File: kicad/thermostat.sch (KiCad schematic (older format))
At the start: 80 parts, among them IC1 LM2596S-5, J1 Conn_01x05, J2 Conn_02x02_Top_Bottom, J3 Conn_01x04, J4 Conn_01x04, J6 Screw_Terminal_01x05, SW1 Button, SW2 Button, SW3 Button, SW4 Button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

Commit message: routed board
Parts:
- removed C11: 25F, Capacitor_THT:CP_Radial_D18.0mm_P7.50mm, symbol Device:CP
- removed C12: 2.2uF, Capacitor_SMD:C_0805_2012Metric, symbol Device:C
- removed C13, C14: 100uF, Capacitor_SMD:C_0805_2012Metric, symbol Device:C
- removed C15, C16: 100nF, Capacitor_SMD:C_0805_2012Metric, symbol Device:C
- removed D44, D45, D46: Green, LED_SMD:LED_0805_2012Metric, symbol Device:LED
- removed J2: Conn_02x02_Top_Bottom, Connector_PinHeader_2.54mm:PinHeader_2x02_P2.54mm_Vertical, symbol Connector_Generic:Conn_02x02_Top_Bottom
- removed L2: 2.2uH, Inductor_SMD:L_Coilcraft_XAL5030, symbol Device:L
- removed R10: 120k, Resistor_SMD:R_0805_2012Metric, symbol Device:R_US
- removed R11: 39k, Resistor_SMD:R_0805_2012Metric, symbol Device:R_US
- removed R12, R44, R45, R46: 1k, Resistor_SMD:R_0805_2012Metric, symbol Device:R_US
- removed R13: 294k, Resistor_SMD:R_0805_2012Metric, symbol Device:R_US
- removed R14: 698k, Resistor_SMD:R_0805_2012Metric, symbol Device:R_US
- removed R15: 1050k, Resistor_SMD:R_0805_2012Metric, symbol Device:R_US
- removed R16: 200k, Resistor_SMD:R_0805_2012Metric, symbol Device:R_US
- removed R18: 10m, Resistor_SMD:R_0805_2012Metric, symbol Device:R_US
- removed T1, T2: SIR434DN, Package_SO:Vishay_PowerPAK_1212-8_Single, symbol Transistor_FET:BUK9M9R1-40EX
- removed U11: LTC4041, project_footprints:ltc4041, symbol thermostat-rescue:LTC4041-thermostat
- added J2: Conn_01x03, Connector_PinHeader_2.54mm:PinHeader_1x03_P2.54mm_Vertical, symbol Connector_Generic:Conn_01x03
- added R57: 10k, Resistor_SMD:R_0805_2012Metric, symbol Device:R_US
- J1: value Conn_01x05 -> Conn_01x04; footprint Connector_PinHeader_2.54mm:PinHeader_1x05_P2.54mm_Vertical -> Connector_PinHeader_2.54mm:PinHeader_1x04_P2.54mm_Vertical; symbol Connector_Generic:Conn_01x05 -> Connector_Generic:Conn_01x04
- J3, J4: value Conn_01x04 -> Conn_01x05; footprint Connector_PinHeader_2.54mm:PinHeader_1x04_P2.54mm_Vertical -> Connector_PinHeader_2.54mm:PinHeader_1x05_P2.54mm_Vertical; symbol Connector_Generic:Conn_01x04 -> Connector_Generic:Conn_01x05
- MK5: footprint MountingHole:MountingHole_5mm_Pad -> MountingHole:MountingHole_5mm
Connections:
- net BTNS_GND: now also J4.3 (Pin_3); no longer J4.2 (Pin_2)
- net BTNS_INT: now also J4.1 (Pin_1), R57.1; no longer U1.15 (INTB)
- net BTNS_PWR_3V3: now also J4.2 (Pin_2); no longer J4.1 (Pin_1)
- net BTNS_SCL: now also J4.5 (Pin_5); no longer J4.4 (Pin_4)
- net BTNS_SDA: now also J4.4 (Pin_4); no longer J4.3 (Pin_3)
- net GND: now also J3.3 (Pin_3), J2.3 (Pin_3); no longer J3.2 (Pin_2)
- net GPIO17(GEN0): now also J3.1 (Pin_1)
- net GPIO2(SDA1): now also J1.3 (Pin_3), J3.4 (Pin_4); no longer J1.4 (Pin_4), J3.3 (Pin_3)
- net GPIO3(SCL1): now also J1.4 (Pin_4), J3.5 (Pin_5); no longer J1.5 (Pin_5), J3.4 (Pin_4)
- net PWR_3.3V: now also J3.2 (Pin_2); no longer J3.1 (Pin_1)
- net PWR_5V: now also J1.2 (Pin_2), J2.2 (Pin_2); no longer J1.3 (Pin_3)
- net PWR_5V_RAW: now also J2.1 (Pin_1)
- net at U1.16 (INTA): now also R57.2
- no-connect marks 35 -> 32
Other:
- note added: "## BMP addr=0x76 ##"
- note added: "## GPIO addr=0x20 ##"
- note added: "## LCD addr=0x27 ##"
- note removed: "## addr=0x20 ##"
- note removed: "## addr=0x27 ##"
- note removed: "## addr=0x76 ##"
- note removed: "*1"
- note removed: "*1) V(chg) = Voltage divider, sets supercap charge voltage\n = 0.8 * (1+698k/294k) = 2.7V\n*2) I(chg) = Resistor program, sets supercap charge current\n = 2000/1k = 1a\n*3) V(in) = Voltage divider, sets input min voltage before power fail\n = 1.19 * (1 + 120k/39k) = 4.85V\n*4) I(syslim) = Resistor program, sets input current limit\n = 25mV/10m = 2.5a\n*5) V(sys) = Voltage divider, sets boost conv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"
- note removed: "*2"
- note removed: "*3"
- note removed: "*4"
- note removed: "*5"
- note removed: "*6"
- moved on the sheet: C1, C2, D1, D2, D40, D41, D42, D43, D47, D51, D52, IC1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

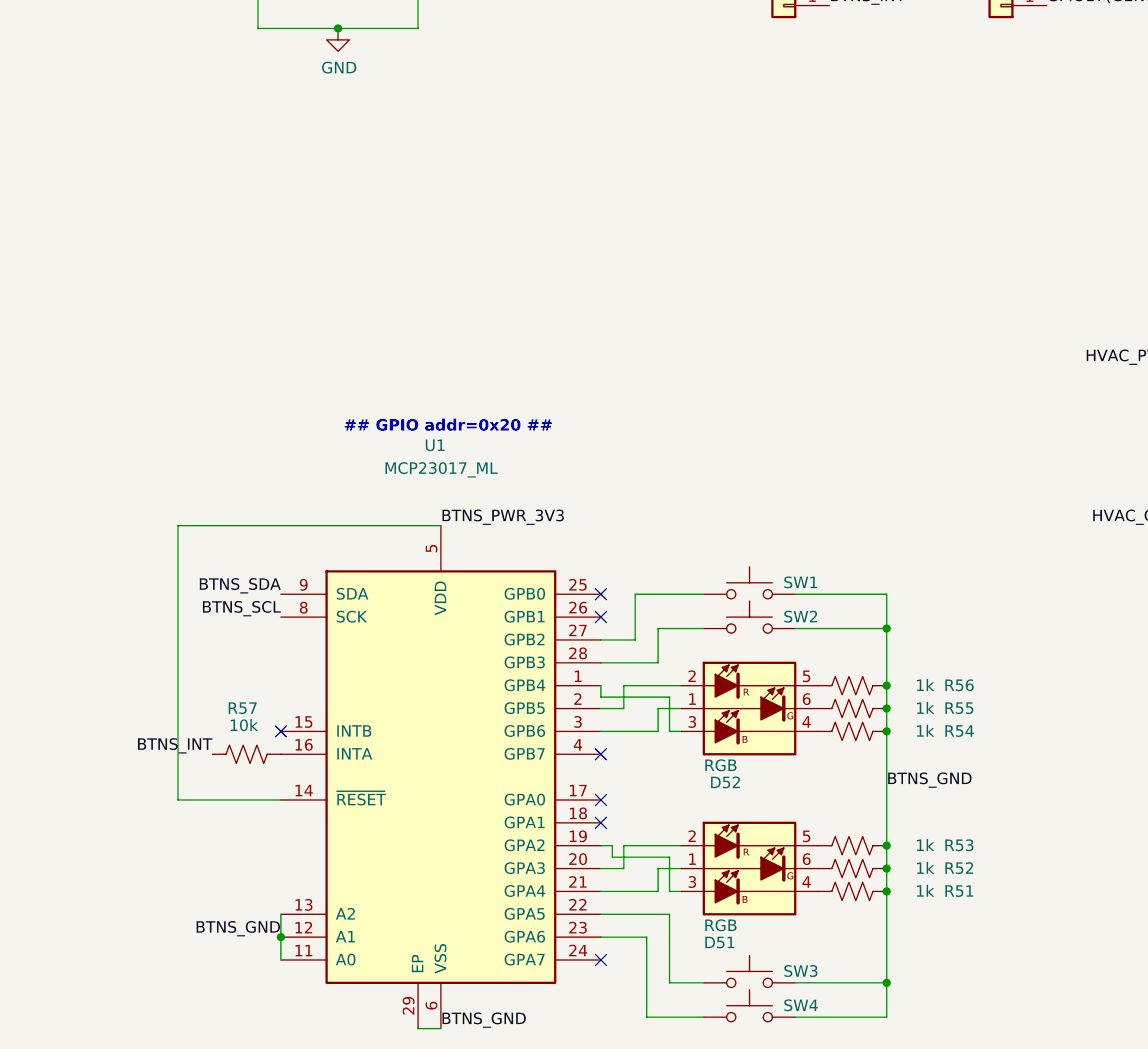
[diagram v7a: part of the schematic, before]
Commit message: moved some diagram objects around
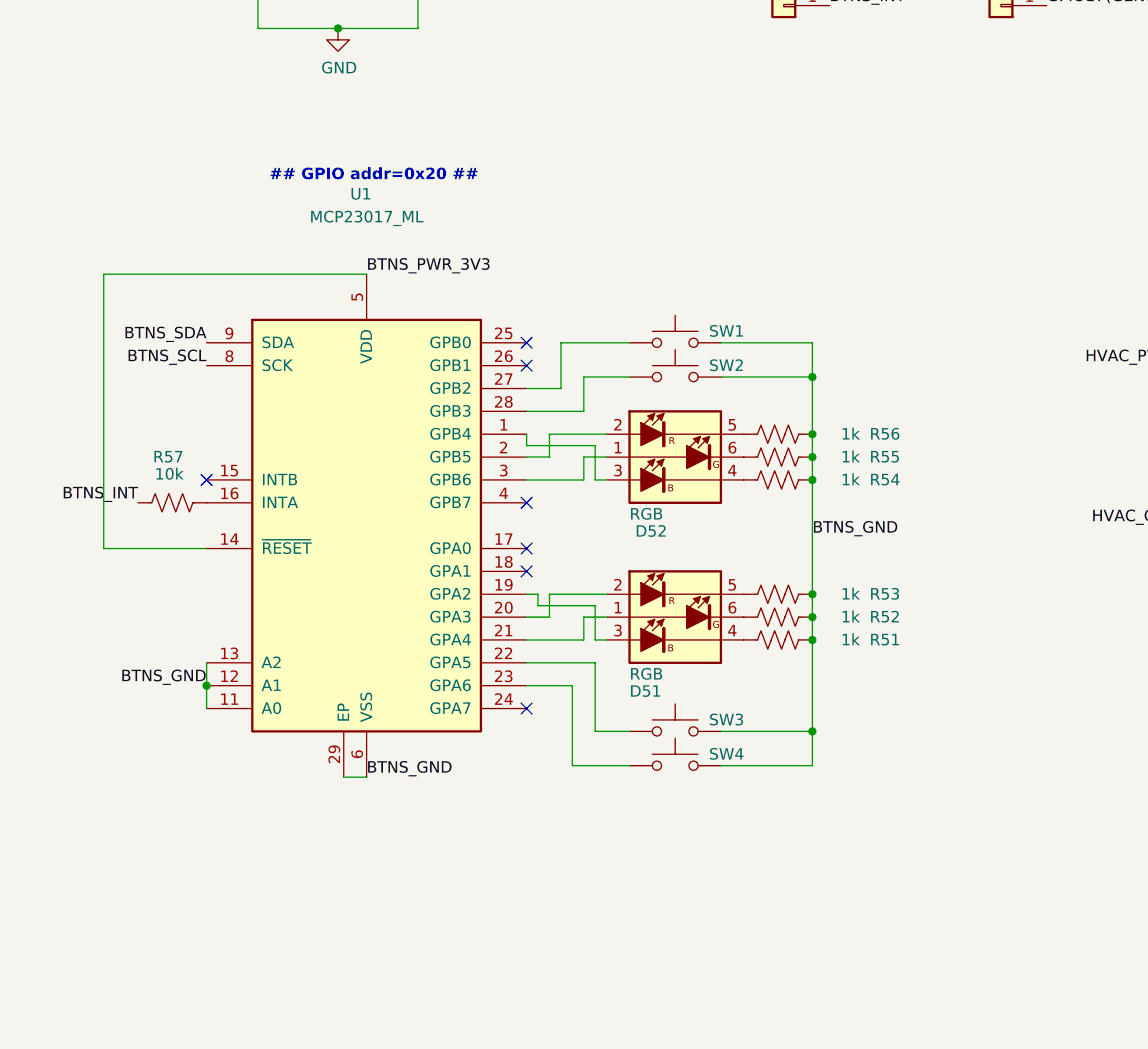
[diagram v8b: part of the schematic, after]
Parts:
- D51, D52: Populate (none) -> 1
- J1, J2, J3, J4, MK1, MK10, MK2, MK3, MK4, MK5, MK7, MK8, MK9: Populate (none) -> 0
- U1: MPN (none) -> 579-MCP23017-E/ML; Mouser (none) -> 579-MCP23017-E/ML; Populate (none) -> 1
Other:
- moved on the sheet: D51, D52, R51, R52, R53, R54, R55, R56, R57, SW1, SW2, SW3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
